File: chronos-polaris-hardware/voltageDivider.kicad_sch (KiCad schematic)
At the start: 6 parts

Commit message: made satvik fixes
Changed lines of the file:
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@@
 	(paper "A4")
+	(junction
+		(at 93.98 71.12)
+		(diameter 0)
+		(color 0 0 0 0)
+	)
 	(junction
 		(at 93.98 87.63)
@@
 	(wire
 		(pts
+			(xy 93.98 71.12) (xy 105.41 71.12)
+		)
+		(stroke
+			(width 0)
+			(type default)
+		)
+	)
+	(wire
+		(pts
 			(xy 100.33 105.41) (xy 119.38 105.41)
 		)
@@
 		(pts
 			(xy 100.33 87.63) (xy 100.33 105.41)
+		)
+		(stroke
+			(width 0)
+			(type default)
+		)
+	)
+	(wire
+		(pts
+			(xy 105.41 72.39) (xy 105.41 71.12)
 		)
 		(stroke
@@
 		)
 	)
-	(global_label "3.3V"
+	(wire
+		(pts
+			(xy 93.98 71.12) (xy 93.98 72.39)
+		)
+		(stroke
+			(width 0)
+			(type default)
+		)
+	)
+	(wire
+		(pts
+			(xy 93.98 69.85) (xy 93.98 71.12)
+		)
+		(stroke
+			(width 0)
+			(type default)
+		)
+	)
+	(hierarchical_label "3.3V"
 		(shape input)
-		(at 105.41 72.39 90)
+		(at 93.98 69.85 90)
 		(fields_autoplaced yes)
 		(effects
@@
 			(justify left)
 		)
-		(property "Intersheetrefs" "${INTERSHEET_REFS}"
-			(at 105.41 65.3718 90)
-			(effects
-				(font
-					(size 1.27 1.27)
-				)
-				(justify left)
-				(hide yes)
-			)
-		)
 	)
-	(global_label "3.3V"
-		(shape input)
-		(at 93.98 72.39 90)
-		(fields_autoplaced yes)
-		(effects
-			(font
-				(size 1.27 1.27)
-			)
-			(justify left)
-		)
-		(property "Intersheetrefs" "${INTERSHEET_REFS}"
-			(at 93.98 65.3718 90)
-			(effects
-				(font
-					(size 1.27 1.27)
-				)
-				(justify left)
-				(hide yes)
-			)
-		)
-	)

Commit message: Fixed warnings and error messages. - Rishik B.
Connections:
- net Drogue Detect renamed DROGUE DETECT
- net Main Detect renamed MAIN DETECT
- net Main V+ renamed MAIN V+
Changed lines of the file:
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@@
 		)
 	)
-	(hierarchical_label "Drogue Detect"
+	(hierarchical_label "DROGUE DETECT"
 		(shape input)
 		(at 118.11 87.63 0)
@@
 		)
 	)
-	(hierarchical_label "Main V+"
+	(hierarchical_label "MAIN V+"
 		(shape input)
 		(at 80.01 80.01 180)
@@
 		)
 	)
-	(hierarchical_label "Main Detect"
+	(hierarchical_label "MAIN DETECT"
 		(shape input)
 		(at 119.38 105.41 0)
@@
 	)
 	(symbol
+		(lib_name "GND_1")
 		(lib_id "power:GND")
 		(at 105.41 95.25 0)
@@
 			)
 		)
-		(property "Description" ""
+		(property "Description" "Power symbol creates a global label with name \"GND\" , ground"
 			(at 105.41 95.25 0)
 			(effects
@@
 	)
 	(symbol
+		(lib_id "Device:R")
+		(at 105.41 83.82 0)
+		(unit 1)
+		(exclude_from_sim no)
+		(in_bom yes)
+		(on_board yes)
+		(dnp no)
+		(property "Reference" "R28"
+			(at 106.68 83.82 0)
+			(effects
+				(font
+					(size 1.27 1.27)
+				)
+				(justify left)
+			)
+		)
+		(property "Value" "30k"
+			(at 106.68 86.36 0)
+			(effects
+				(font
+					(size 1.27 1.27)
+				)
+				(justify left)
+			)
+		)
+		(property "Footprint" "Resistor_SMD:R_0603_1608Metric"
+			(at 103.632 83.82 90)
+			(effects
+				(font
+					(size 1.27 1.27)
+				)
+				(hide yes)
+			)
+		)
+		(property "Datasheet" "~"
+			(at 105.41 83.82 0)
+			(effects
+				(font
+					(size 1.27 1.27)
+				)
+				(hide yes)
+			)
+		)
+		(property "Description" ""
+			(at 105.41 83.82 0)
+			(effects
+				(font
+					(size 1.27 1.27)
+				)
+				(hide yes)
+			)
+		)
+		(pin "1"
+		)
+		(pin "2"
+		)
+		(instances
+			(project "chronos-polaris-hardware"
+				(path "/503f01d5-a0c6-4ade-b485-97c3c2e1d6c5/97b61835-1bd5-4048-92e6-24e014b2d83b"
+					(reference "R28")
+					(unit 1)
+				)
+			)
+		)
+	)
+	(symbol
+		(lib_id "Device:R")
+		(at 105.41 76.2 0)
+		(unit 1)
+		(exclude_from_sim no)
+		(in_bom yes)
+		(on_board yes)
+		(dnp no)
+		(property "Reference" "R27"
+			(at 106.68 76.2 0)
+			(effects
+				(font
+					(size 1.27 1.27)
+				)
+				(justify left)
+			)
+		)
+		(property "Value" "10k"
+			(at 106.68 78.74 0)
+			(effects
+				(font
+					(size 1.27 1.27)
+				)
+				(justify left)
+			)
+		)
+		(property "Footprint" "Resistor_SMD:R_0603_1608Metric"
+			(at 103.632 76.2 90)
+			(effects
+				(font
+					(size 1.27 1.27)
+				)
+				(hide yes)
+			)
+		)
+		(property "Datasheet" "~"
+			(at 105.41 76.2 0)
+			(effects
+				(font
+					(size 1.27 1.27)
+				)
+				(hide yes)
+			)
+		)
+		(property "Description" ""
+			(at 105.41 76.2 0)
+			(effects
+				(font
+					(size 1.27 1.27)
+				)
+				(hide yes)
+			)
+		)
+		(pin "1"
+		)
+		(pin "2"
+		)
+		(instances
+			(project "chronos-polaris-hardware"
+				(path "/503f01d5-a0c6-4ade-b485-97c3c2e1d6c5/97b61835-1bd5-4048-92e6-24e014b2d83b"
+					(reference "R27")
+					(unit 1)
+				)
+			)
+		)
+	)
+	(symbol
+		(lib_id "Device:R")
+		(at 105.41 91.44 0)
+		(unit 1)
+		(exclude_from_sim no)
+		(in_bom yes)
+		(on_board yes)
+		(dnp no)
+		(property "Reference" "R29"
+			(at 106.68 91.44 0)
+			(effects
+				(font
+					(size 1.27 1.27)
+				)
+				(justify left)
+			)
+		)
+		(property "Value" "10k"
+			(at 106.68 93.98 0)
+			(effects
+				(font
+					(size 1.27 1.27)
+				)
+				(justify left)
+			)
+		)
+		(property "Footprint" "Resistor_SMD:R_0603_1608Metric"
+			(at 103.632 91.44 90)
+			(effects
+				(font
+					(size 1.27 1.27)
+				)
+				(hide yes)
+			)
+		)
+		(property "Datasheet" "~"
+			(at 105.41 91.44 0)
+			(effects
+				(font
+					(size 1.27 1.27)
+				)
+				(hide yes)
+			)
+		)
+		(property "Description" ""
+			(at 105.41 91.44 0)
+			(effects
+				(font
+					(size 1.27 1.27)
+				)
+				(hide yes)
+			)
+		)
+		(pin "1"
+		)
+		(pin "2"
+		)
+		(instances
+			(project "chronos-polaris-hardware"
+				(path "/503f01d5-a0c6-4ade-b485-97c3c2e1d6c5/97b61835-1bd5-4048-92e6-24e014b2d83b"
+					(reference "R29")
+					(unit 1)
+				)
+			)
+		)
+	)
+	(symbol
+		(lib_name "GND_1")
 		(lib_id "power:GND")
 		(at 93.98 95.25 0)
@@
 			)
 		)
-		(property "Description" ""
+		(property "Description" "Power symbol creates a global label with name \"GND\" , ground"
 			(at 93.98 95.25 0)
 			(effects
@@
 					(unit 1)
 				)
-			)
-		)
-	)
-	(symbol
-		(lib_id "Device:R")
-		(at 105.41 83.82 0)
-		(unit 1)
-		(exclude_from_sim no)
-		(in_bom yes)
-		(on_board yes)
-		(dnp no)
-		(property "Reference" "R28"
-			(at 106.68 83.82 0)
-			(effects
-				(font
-					(size 1.27 1.27)
-				)
-				(justify left)
-			)
-		)
-		(property "Value" "30k"
-			(at 106.68 86.36 0)
-			(effects
-				(font
-					(size 1.27 1.27)
-				)
-				(justify left)
-			)
-		)
-		(property "Footprint" "Resistor_SMD:R_0603_1608Metric"
-			(at 103.632 83.82 90)
-			(effects
-				(font
-					(size 1.27 1.27)
-				)
-				(hide yes)
-			)
-		)
-		(property "Datasheet" "~"
-			(at 105.41 83.82 0)
-			(effects
-				(font
-					(size 1.27 1.27)
-				)
-				(hide yes)
-			)
-		)
-		(property "Description" ""
-			(at 105.41 83.82 0)
-			(effects
-				(font
-					(size 1.27 1.27)
-				)
-				(hide yes)
-			)
-		)
-		(pin "1"
-		)
-		(pin "2"
-		)
-		(instances
-			(project "chronos-polaris-hardware"
-				(path "/503f01d5-a0c6-4ade-b485-97c3c2e1d6c5/97b61835-1bd5-4048-92e6-24e014b2d83b"
-					(reference "R28")
-					(unit 1)
-				)
-			)
-		)
-	)
-	(symbol
-		(lib_id "Device:R")
-		(at 105.41 76.2 0)
-		(unit 1)
-		(exclude_from_sim no)
-		(in_bom yes)
-		(on_board yes)
-		(dnp no)
-		(property "Reference" "R27"
-			(at 106.68 76.2 0)
-			(effects
-				(font
-					(size 1.27 1.27)
-				)
-				(justify left)
-			)
-		)
-		(property "Value" "10k"
-			(at 106.68 78.74 0)
-			(effects
-				(font
-					(size 1.27 1.27)
-				)
-				(justify left)
-			)
-		)
-		(property "Footprint" "Resistor_SMD:R_0603_1608Metric"
-			(at 103.632 76.2 90)
-			(effects
-				(font
-					(size 1.27 1.27)
-				)
-				(hide yes)
-			)
-		)
-		(property "Datasheet" "~"
-			(at 105.41 76.2 0)
-			(effects
-				(font
-					(size 1.27 1.27)
-				)
-				(hide yes)
-			)
-		)
-		(property "Description" ""
-			(at 105.41 76.2 0)
-			(effects
-				(font
-					(size 1.27 1.27)
-				)
-				(hide yes)
-			)
-		)
-		(pin "1"
-		)
-		(pin "2"
-		)
-		(instances
-			(project "chronos-polaris-hardware"
-				(path "/503f01d5-a0c6-4ade-b485-97c3c2e1d6c5/97b61835-1bd5-4048-92e6-24e014b2d83b"
-					(reference "R27")
-					(unit 1)
-				)
-			)
-		)
-	)
-	(symbol
-		(lib_id "Device:R")
-		(at 105.41 91.44 0)
-		(unit 1)
-		(exclude_from_sim no)
-		(in_bom yes)
-		(on_board yes)
-		(dnp no)
-		(property "Reference" "R29"
-			(at 106.68 91.44 0)
-			(effects
-				(font
-					(size 1.27 1.27)
-				)
-				(justify left)
-			)
-		)
-		(property "Value" "10k"
-			(at 106.68 93.98 0)
-			(effects
-				(font
-					(size 1.27 1.27)
-				)
-				(justify left)
-			)
-		)
-		(property "Footprint" "Resistor_SMD:R_0603_1608Metric"
-			(at 103.632 91.44 90)
-			(effects
-				(font
-					(size 1.27 1.27)
-				)
-				(hide yes)
-			)
-		)
-		(property "Datasheet" "~"
-			(at 105.41 91.44 0)
-			(effects
-				(font
-					(size 1.27 1.27)
-				)
-				(hide yes)
-			)
-		)
-		(property "Description" ""
-			(at 105.41 91.44 0)
-			(effects
-				(font
-					(size 1.27 1.27)
-				)
-				(hide yes)
-			)
-		)
-		(pin "1"
-		)
-		(pin "2"
-		)
-		(instances
-			(project "chronos-polaris-hardware"
-				(path "/503f01d5-a0c6-4ade-b485-97c3c2e1d6c5/97b61835-1bd5-4048-92e6-24e014b2d83b"
-					(reference "R29")
-					(unit 1)
-				)

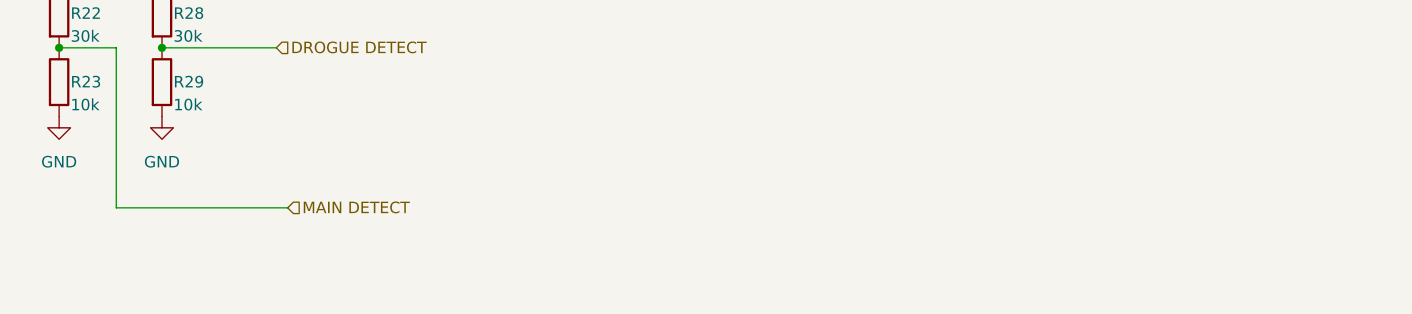
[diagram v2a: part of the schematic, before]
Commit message: Schematic Changes as per DR1 Suggestions
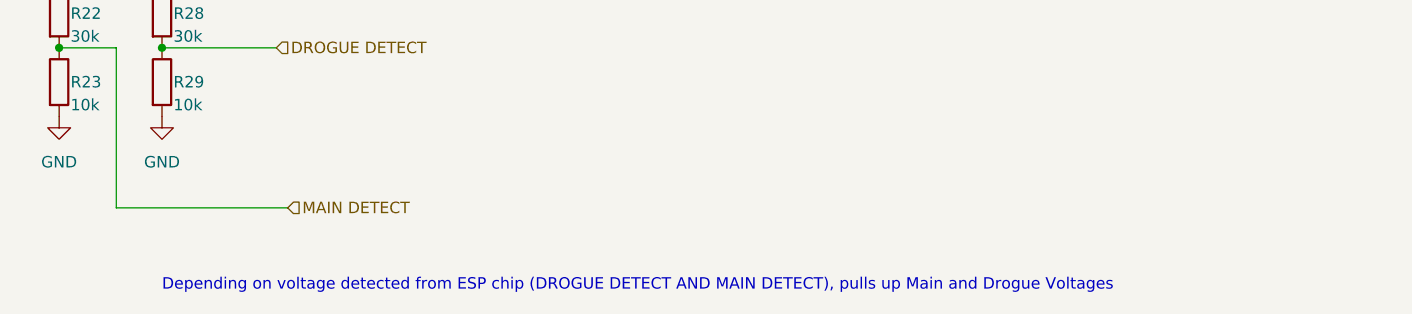
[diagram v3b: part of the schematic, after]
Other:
- note added: "Depending on voltage detected from ESP chip (DROGUE DETECT AND MAIN DETECT), pulls up Main and Drogue Voltages"
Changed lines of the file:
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@@
+		)
+	)
+	(text "Depending on voltage detected from ESP chip (DROGUE DETECT AND MAIN DETECT), pulls up Main and Drogue Voltages"
+		(exclude_from_sim no)
+		(at 105.41 114.046 0)
+		(effects
+			(font
+				(size 1.27 1.27)
+			)
+			(justify left)
 		)
 	)

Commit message: fixes. - Rishik B.
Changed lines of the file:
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@@
 	)
 	(hierarchical_label "DROGUE DETECT"
-		(shape input)
+		(shape output)
 		(at 118.11 87.63 0)
 		(fields_autoplaced yes)
@@
 	)
 	(hierarchical_label "MAIN DETECT"
-		(shape input)
+		(shape output)
 		(at 119.38 105.41 0)
 		(fields_autoplaced yes)
